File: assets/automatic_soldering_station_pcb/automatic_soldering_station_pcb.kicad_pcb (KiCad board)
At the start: 2 copper layers, 100 x 130 mm, 24 parts, among them J1 XY_MOS, J2 MAX6675, J3 MAX6675, J4 MAX6675

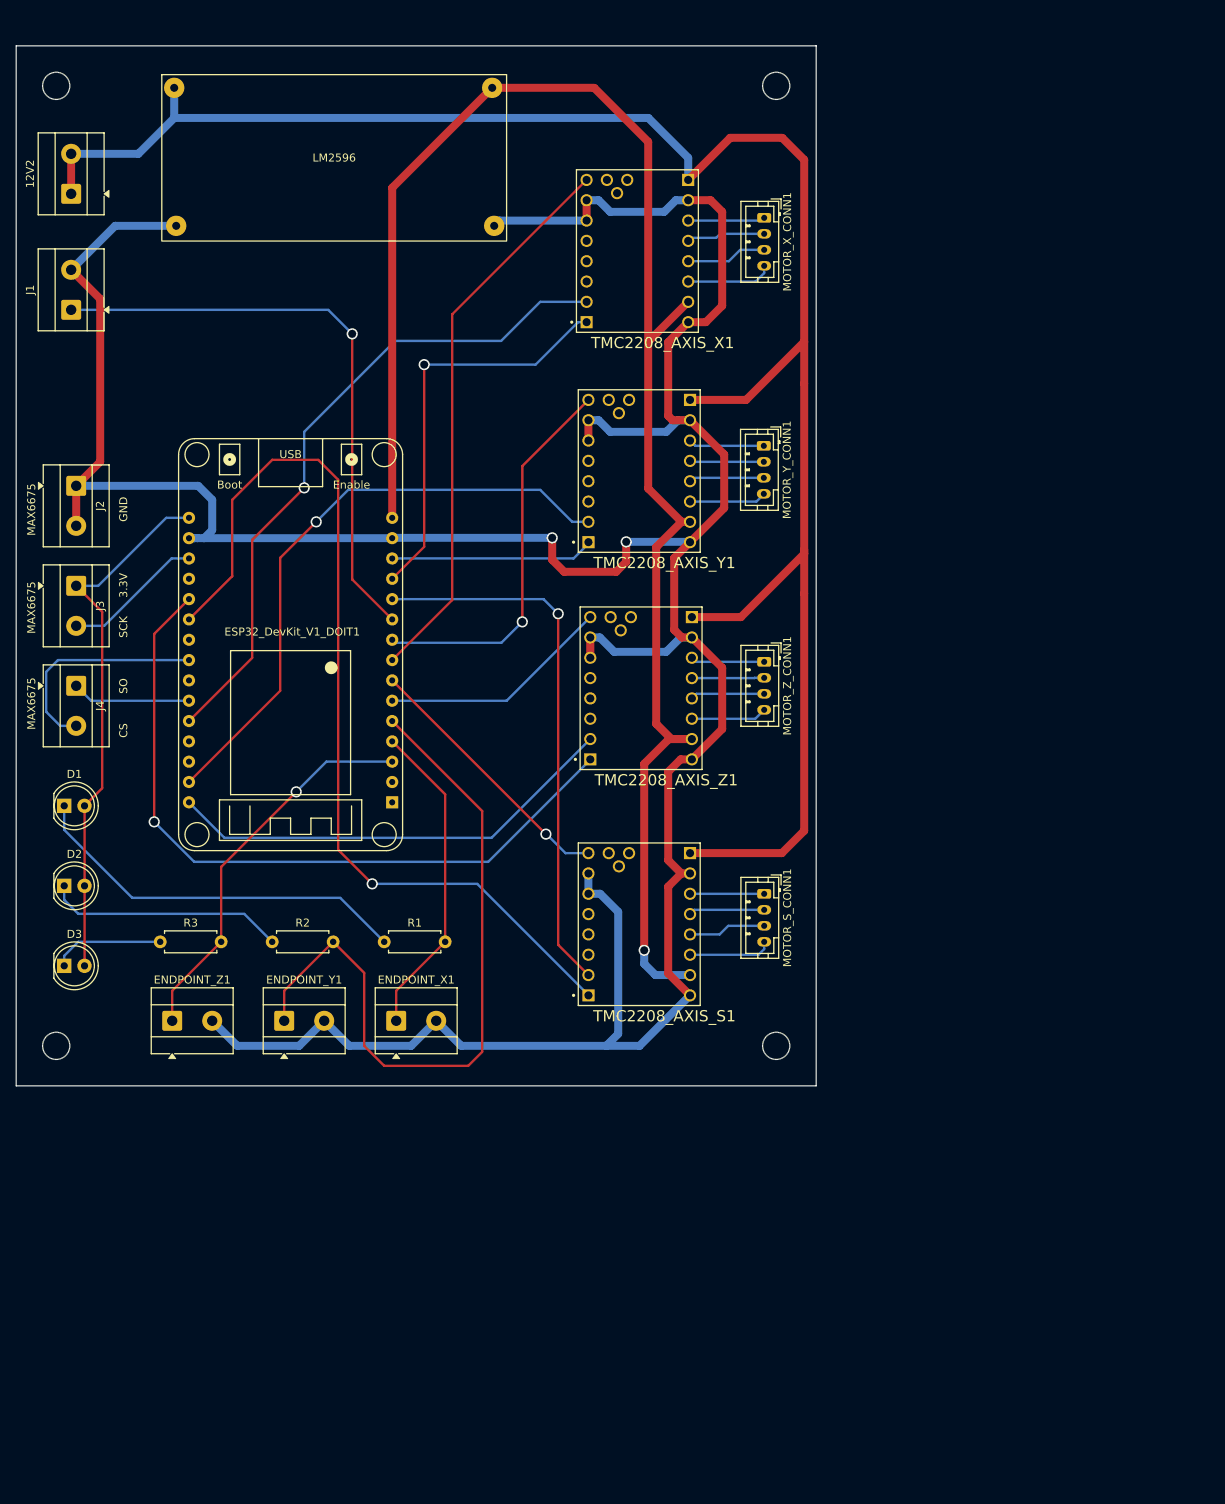
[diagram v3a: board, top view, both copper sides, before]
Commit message: pcb: fix printer specific mistakes
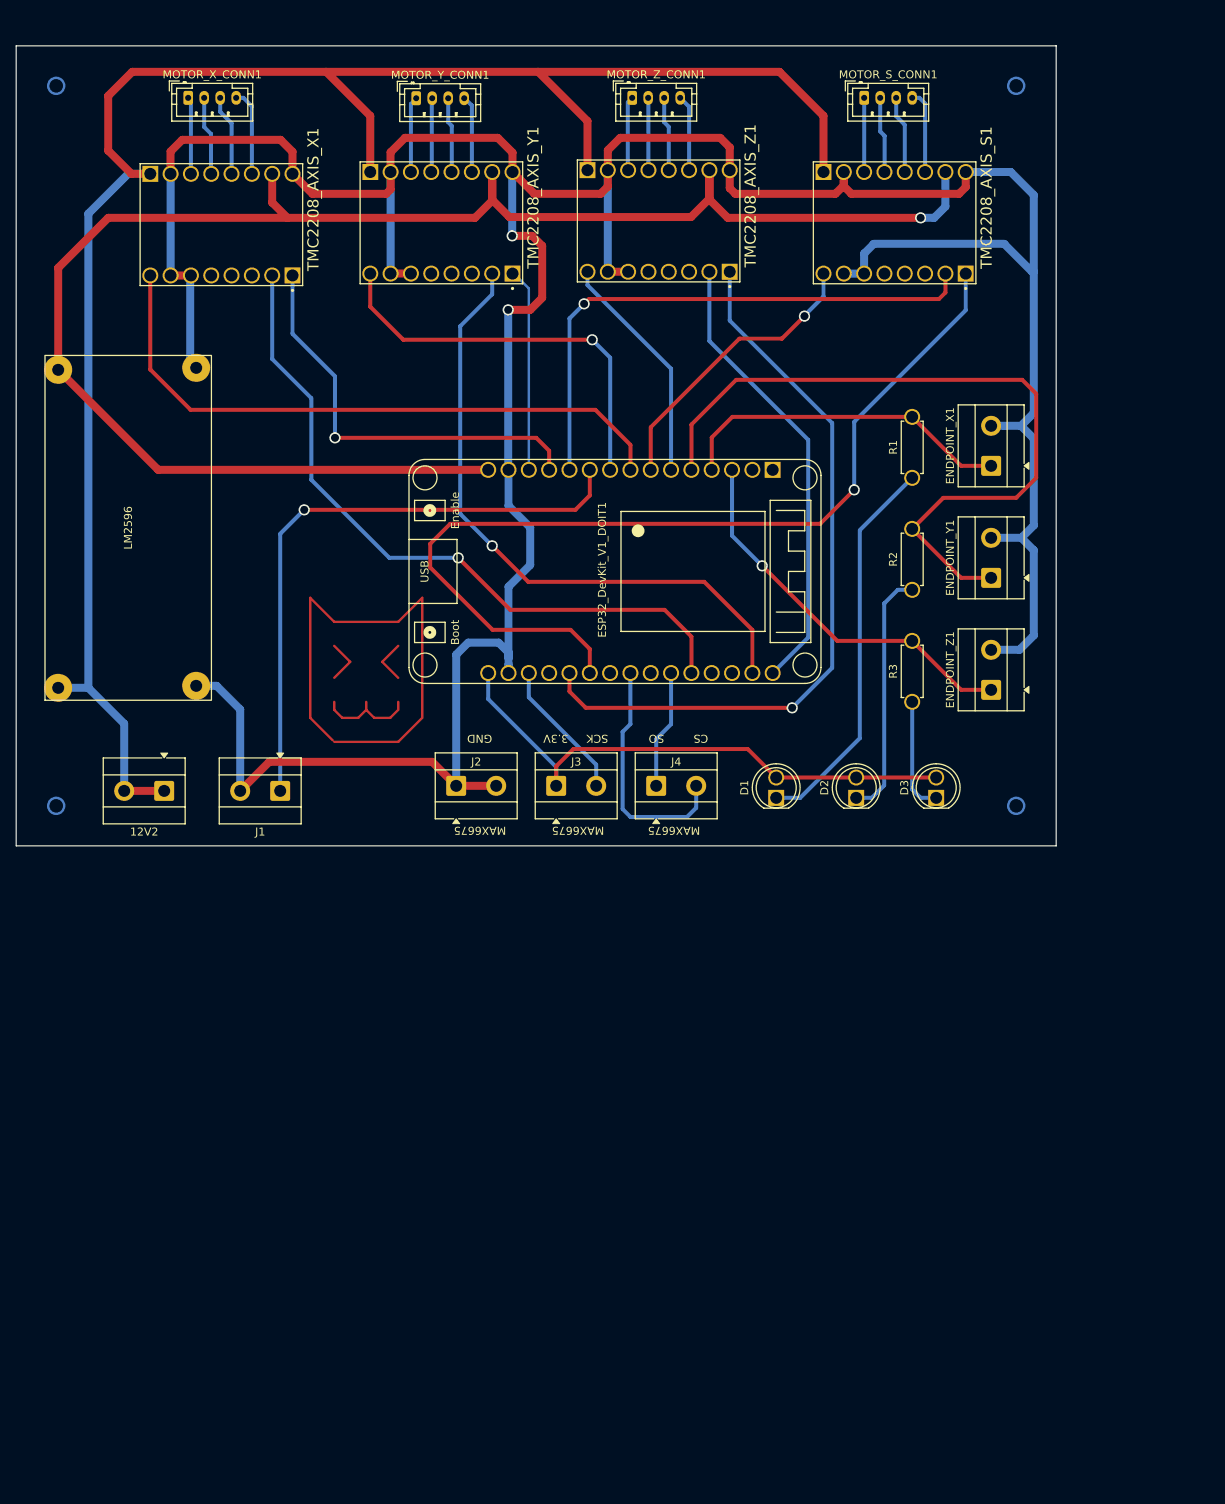
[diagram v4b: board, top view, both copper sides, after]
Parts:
- moved D3 111.0 mm to (127.0, 106.0), turned to 90 degrees
- moved ENDPOINT_Z1 110.4 mm to (133.9, 92.5), turned to 90 degrees
- moved ENDPOINT_Y1 104.3 mm to (133.9, 78.5), turned to 90 degrees
- moved ENDPOINT_X1 101.7 mm to (133.9, 64.5), turned to 90 degrees
- moved MOTOR_S_CONN1 100.3 mm to (118.0, 18.5), turned to 0 degrees
- moved D2 99.6 mm to (117.0, 106.0), turned to 90 degrees
- moved R3 98.7 mm to (124.0, 94.0), turned to 90 degrees
- moved TMC2208_AXIS_S1 93.3 mm to (121.8, 34.1), turned to -90 degrees
- moved R2 91.3 mm to (124.0, 80.0), turned to 90 degrees
- moved D1 89.0 mm to (107.0, 106.0), turned to 90 degrees
- moved R1 87.9 mm to (124.0, 66.0), turned to 90 degrees
- moved 12V2 75.5 mm to (30.5, 105.1), turned to 180 degrees
- moved J4 73.6 mm to (92.0, 104.5), turned to 0 degrees
- moved MOTOR_X_CONN1 73.5 mm to (33.5, 18.5), turned to 0 degrees
- moved MOTOR_Z_CONN1 72.4 mm to (89.0, 18.5), turned to 0 degrees
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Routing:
- net (no net): track 0.00 -> 86.7 mm
- net GND: track 421.2 -> 448.5 mm
- net +12V: track 244.8 -> 235.5 mm
- net /X_EN: track 70.1 -> 78.8 mm
- net +5V: track 208.9 -> 213.3 mm
- net /X_STEP: track 84.1 -> 87.7 mm
- net /Y_ENDPOINT: track 89.5 -> 92.8 mm
- net /Y_STEP: track 76.4 -> 79.6 mm
- net /S_EN: track 33.5 -> 36.6 mm
- net +3.3V: track 67.4 -> 69.9 mm
- net /X_ENDPOINT: track 40.4 -> 42.7 mm
- net /MAX6675_CS: track 27.9 -> 30.2 mm
- net /Y_EN: track 48.7 -> 50.8 mm
- net /XY_MOS_PWM: track 74.1 -> 76.0 mm
- net /X_DIR: track 50.9 -> 52.3 mm
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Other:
- board size 100 x 130 mm -> 130 x 100 mm

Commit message: pcb: reduce size of pcb
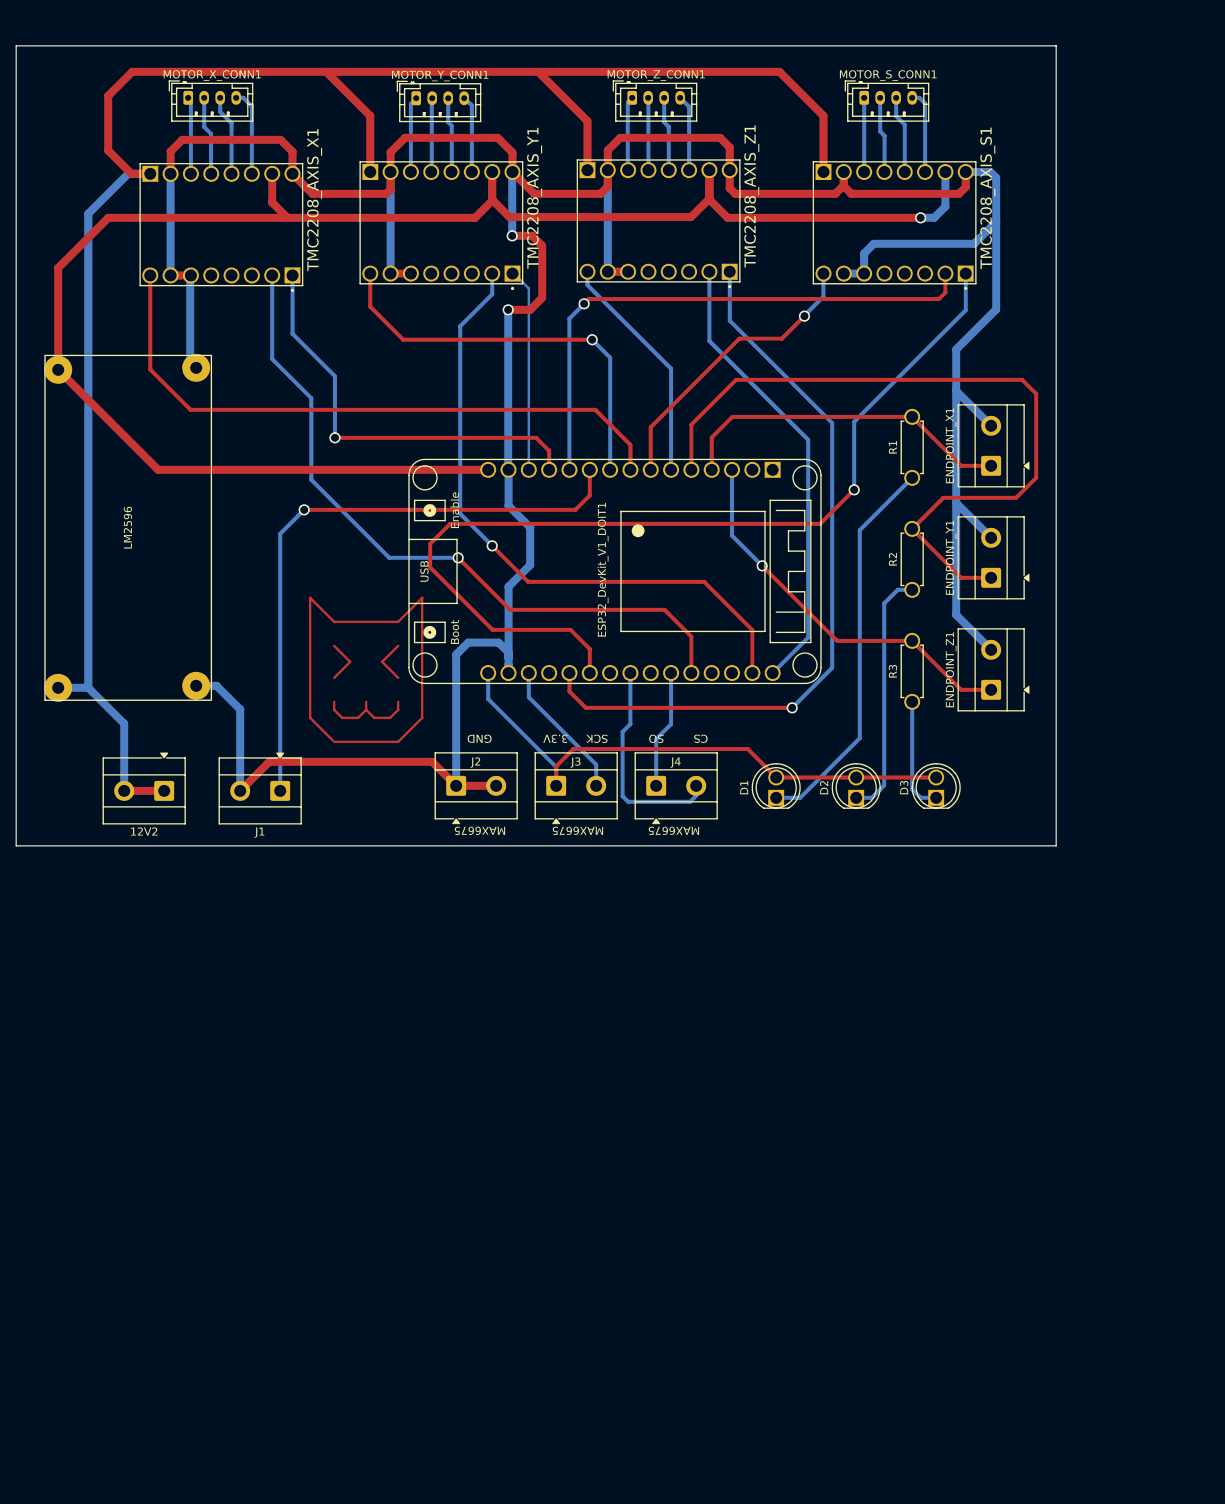
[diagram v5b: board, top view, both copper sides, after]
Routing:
- net GND: track 448.5 -> 441.9 mm
- net /MAX6675_CS: track 30.2 -> 26.9 mm
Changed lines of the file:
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@@
 		(embedded_fonts no)
-	)
-	(gr_circle
-		(center 17 17)
-		(end 18 17)
-		(stroke
-			(width 0.3)
-			(type solid)
-		)
-		(fill no)
-		(layer "B.Cu")
-	)
-	(gr_circle
-		(center 17 107)
-		(end 18 107)
-		(stroke
-			(width 0.3)
-			(type solid)
-		)
-		(fill no)
-		(layer "B.Cu")
-	)
-	(gr_circle
-		(center 137 17)
-		(end 138 17)
-		(stroke
-			(width 0.3)
-			(type solid)
-		)
-		(fill no)
-		(layer "B.Cu")
-	)
-	(gr_circle
-		(center 137 107)
-		(end 138 107)
-		(stroke
-			(width 0.3)
-			(type solid)
-		)
-		(fill no)
-		(layer "B.Cu")
 	)
 	(gr_rect
@@
 	)
 	(segment
+		(start 131.75 36.75)
+		(end 134.5 34)
+		(width 1)
+		(layer "B.Cu")
+		(net 1)
+	)
+	(segment
 		(start 67 104.5)
 		(end 67 88.1)
@@
 	)
 	(segment
-		(start 139.2 57.9)
-		(end 137.6 59.5)
+		(start 130.691 27.77)
+		(end 133.77 27.77)
 		(width 1)
 		(layer "B.Cu")
@@
 	)
 	(segment
+		(start 134.5 44.95)
+		(end 129.5 49.95)
+		(width 1)
+		(layer "B.Cu")
+		(net 1)
+	)
+	(segment
 		(start 117.991 40.47)
 		(end 115.451 40.47)
@@
 	)
 	(segment
+		(start 119.2 36.75)
+		(end 131.75 36.75)
+		(width 1)
+		(layer "B.Cu")
+		(net 1)
+	)
+	(segment
+		(start 129.5 69.1325)
+		(end 133.8675 73.5)
+		(width 1)
+		(layer "B.Cu")
+		(net 1)
+	)
+	(segment
 		(start 74 27.81)
 		(end 74.04 27.77)
@@
 	)
 	(segment
-		(start 137.4 87.5)
-		(end 139.2 85.7)
-		(width 1)
-		(layer "B.Cu")
-		(net 1)
-	)
-	(segment
-		(start 137.6 59.5)
-		(end 139.2 61.1)
+		(start 134.5 34)
+		(end 134.5 44.95)
 		(width 1)
 		(layer "B.Cu")
@@
 	)
 	(segment
+		(start 129.5 83.1325)
+		(end 133.8675 87.5)
+		(width 1)
+		(layer "B.Cu")
+		(net 1)
+	)
+	(segment
 		(start 76.25 72.2)
 		(end 73.54 69.49)
@@
 	)
 	(segment
-		(start 130.691 27.77)
-		(end 136.32 27.77)
+		(start 129.5 69.1325)
+		(end 129.5 83.1325)
 		(width 1)
 		(layer "B.Cu")
@@
 	)
 	(segment
-		(start 139.2 85.7)
-		(end 139.2 75.05)
-		(width 1)
-		(layer "B.Cu")
-		(net 1)
-	)
-	(segment
 		(start 73.54 89.7395)
 		(end 73.54 89.6982)
@@
 	)
 	(segment
-		(start 139.2 40.25)
-		(end 139.2 57.9)
-		(width 1)
-		(layer "B.Cu")
-		(net 1)
-	)
-	(segment
-		(start 139.2 30.65)
-		(end 139.2 40.25)
-		(width 1)
-		(layer "B.Cu")
-		(net 1)
-	)
-	(segment
-		(start 135.55 59.5)
-		(end 137.6 59.5)
-		(width 1)
-		(layer "B.Cu")
-		(net 1)
-	)
-	(segment
-		(start 139 40.25)
-		(end 139.2 40.25)
+		(start 129.5 49.95)
+		(end 129.5 55.1325)
 		(width 1)
 		(layer "B.Cu")
@@
 	)
 	(segment
-		(start 135.5 36.75)
-		(end 119.2 36.75)
-		(width 1)
-		(layer "B.Cu")
-		(net 1)
-	)
-	(segment
 		(start 74 35.75)
 		(end 74 27.81)
@@
 	)
 	(segment
-		(start 139.2 75.05)
-		(end 137.65 73.5)
-		(width 1)
-		(layer "B.Cu")
-		(net 1)
-	)
-	(segment
 		(start 73.54 79.61)
 		(end 76.25 76.9)
@@
 	)
 	(segment
-		(start 137.65 73.5)
-		(end 133.8675 73.5)
-		(width 1)
-		(layer "B.Cu")
-		(net 1)
-	)
-	(segment
 		(start 67 88.1)
 		(end 68.5 86.6)
@@
 	)
 	(segment
-		(start 139.2 71.95)
-		(end 137.65 73.5)
+		(start 134.5 28.5)
+		(end 134.5 34)
+		(width 1)
+		(layer "B.Cu")
+		(net 1)
+	)
+	(segment
+		(start 129.5 55.1325)
+		(end 129.5 69.1325)
 		(width 1)
 		(layer "B.Cu")
@@
 	)
 	(segment
+		(start 133.77 27.77)
+		(end 134.5 28.5)
+		(width 1)
+		(layer "B.Cu")
+		(net 1)
+	)
+	(segment
+		(start 129.5 55.1325)
+		(end 133.8675 59.5)
+		(width 1)
+		(layer "B.Cu")
+		(net 1)
+	)
+	(segment
 		(start 33.75 40.79)
 		(end 33.75 51.5)
@@
 	)
 	(segment
-		(start 136.32 27.77)
-		(end 139.2 30.65)
-		(width 1)
-		(layer "B.Cu")
-		(net 1)
-	)
-	(segment
-		(start 135.5 36.75)
-		(end 139 40.25)
-		(width 1)
-		(layer "B.Cu")
-		(net 1)
-	)
-	(segment
 		(start 85.951 27.54)
 		(end 85.951 40.24)
@@
 	)
 	(segment
-		(start 133.8675 87.5)
-		(end 137.4 87.5)
-		(width 1)
-		(layer "B.Cu")
-		(net 1)
-	)
-	(segment
 		(start 73.54 87.84)
 		(end 73.54 88.5)
-		(width 1)
-		(layer "B.Cu")
-		(net 1)
-	)
-	(segment
-		(start 133.8675 59.5)
-		(end 135.55 59.5)
-		(width 1)
-		(layer "B.Cu")
-		(net 1)
-	)
-	(segment
-		(start 139.2 61.1)
-		(end 139.2 71.95)
 		(width 1)
 		(layer "B.Cu")
@@
 	)
 	(segment
-		(start 95.85 108.4)
-		(end 97 107.25)
+		(start 87.8 105.8)
+		(end 88.5 106.5)
 		(width 0.5)
 		(layer "B.Cu")
@@
 	)
 	(segment
-		(start 87.8 97.75)
-		(end 87.8 107.4)
+		(start 97 105.75)
+		(end 97 104.5)
 		(width 0.5)
 		(layer "B.Cu")
@@
 	)
 	(segment
-		(start 97 107.25)
-		(end 97 104.5)
+		(start 96.25 106.5)
+		(end 97 105.75)
 		(width 0.5)
 		(layer "B.Cu")
@@
 	)
 	(segment
-		(start 87.8 107.4)
-		(end 88.8 108.4)
+		(start 87.8 97.75)
+		(end 87.8 105.8)
 		(width 0.5)
 		(layer "B.Cu")
@@
 	)
 	(segment
-		(start 88.8 108.4)
-		(end 95.85 108.4)
-		(width 0.5)
-		(layer "B.Cu")
+		(start 88.5 106.5)
+		(end 96.25 106.5)
+		(width 0.5)
+		(layer "B.Cu")
